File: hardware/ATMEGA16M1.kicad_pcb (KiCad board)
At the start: 2 copper layers, 114.3 x 101.6 mm, 65 parts, among them IC1 ATMEGA16M1-A, IC2 MCP2551-I/SN, J1 PWR, J2 USB, J3 RELAY1, J4 RELAY2, J5 RELAY3, J6 GPIO, J7 AMP/D2A, J8 ADC, J9 CAN, SW1 RESET, U1 NCP1117ST50T3G, U2 FT232RL, U3 RELAY_VO14642AT, U4 RELAY_VO14642AT, U5 RELAY_VO14642AT, X1 16MHz

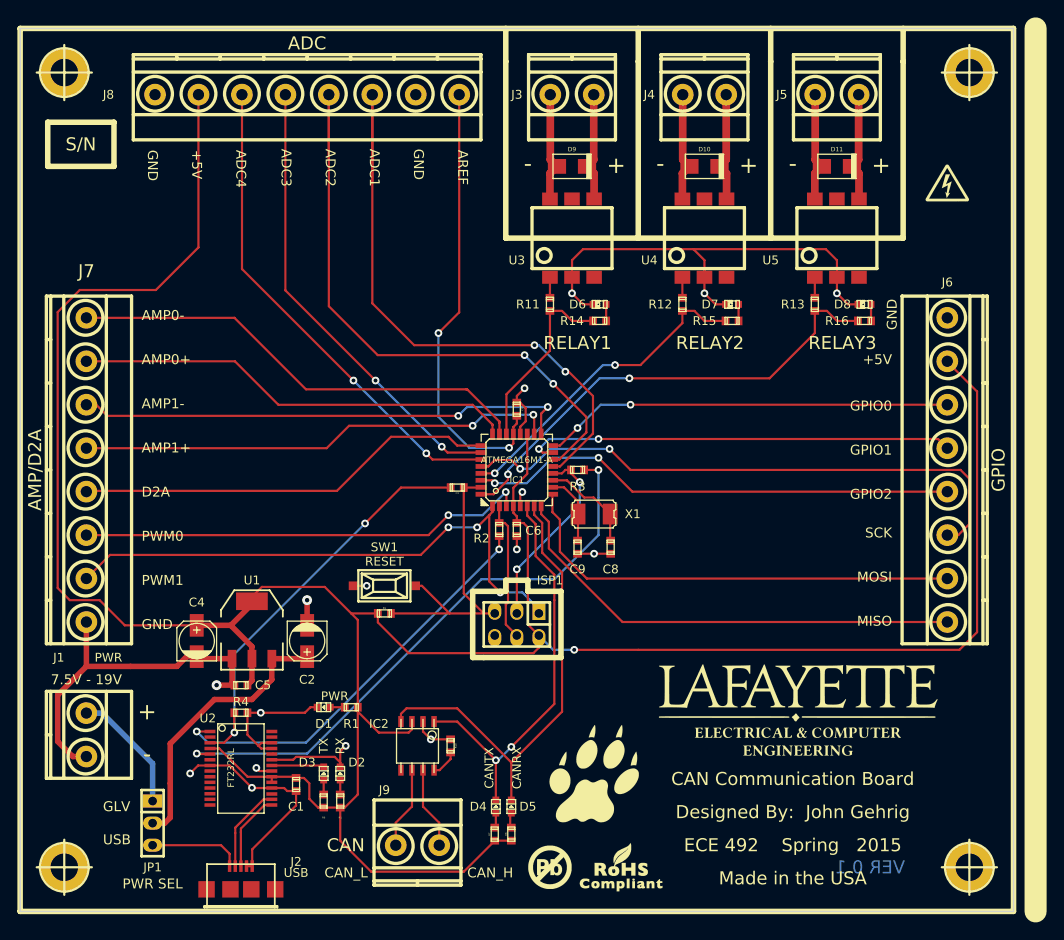
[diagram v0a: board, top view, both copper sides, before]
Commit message: FTDI <-> ISP issue addressed, dip switch added
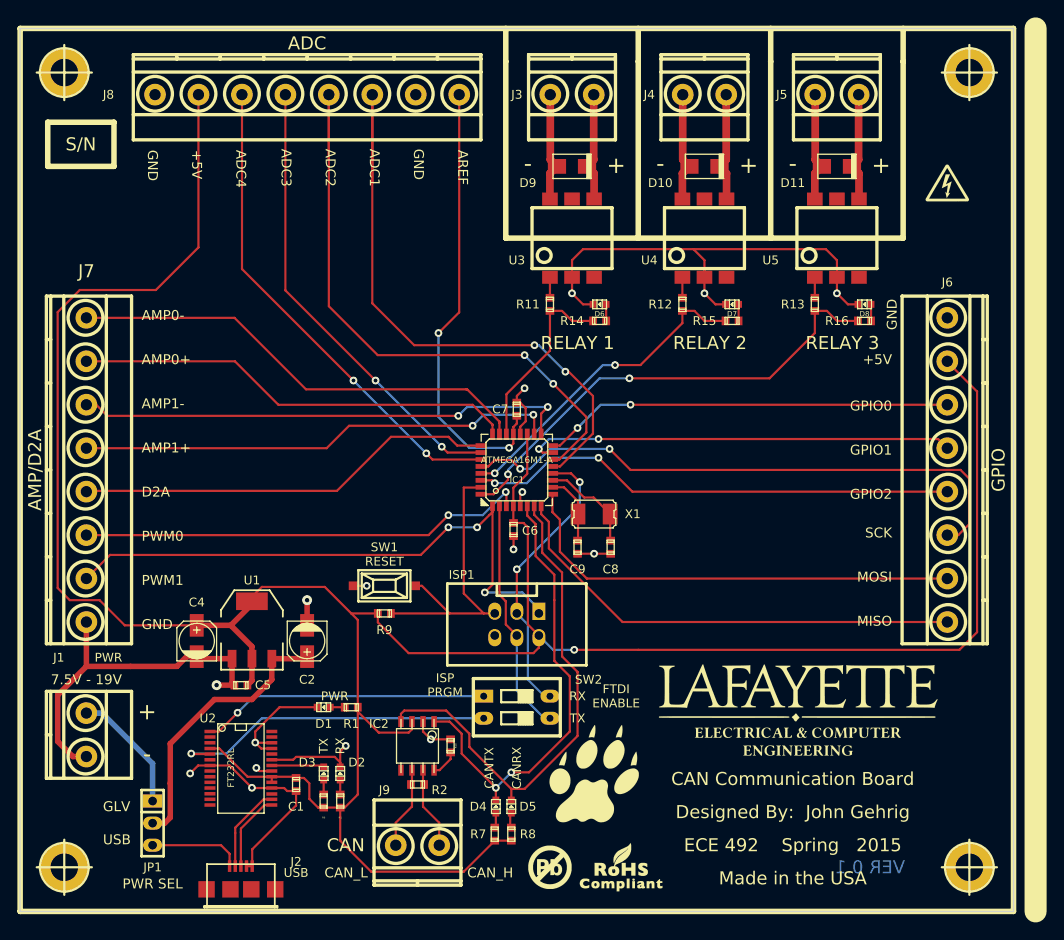
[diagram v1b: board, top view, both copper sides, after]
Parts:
- removed C3: 0.1u, c_0603
- removed R3, R4: 1k, r_0603
- added SW2: FTDI, dip_2-300, F.Cu at (100.3, 123.8)
- C1: value C -> 0.1u
- C5: value 0.1 -> 0.1u
- C8, C9: value 22p -> 10p
- D6, D7, D8: footprint LED-0603 -> Led_0603
- ISP1: footprint pin_strip_3x2 -> vasch_strip_3x2
- J3: value RELAY1 -> RELAY 1
- J4: value RELAY2 -> RELAY 2
- J5: value RELAY3 -> RELAY 3
- R2: value 1k -> 120
- moved R2 30.8 mm to (88.9, 132.7), turned to 0 degrees
- moved C6 0.38 mm to (99.9, 103.4)
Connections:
- R2 pad 1: /FTDI_TX -> /CAN_H
- R2 pad 2: /MOSI_A -> /CAN_L
- U2 pad 3: /RTS -> (no net)
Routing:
- net /RTS: track 47.5 -> 0.00 mm, vias 2 -> 0
- net /FTDI_RX: track 67.3 -> 37.5 mm, vias 2 -> 1
- net /FTDI_TX: track 47.7 -> 33.2 mm, vias 2 -> 1
- net /RXD: track 22.2 -> 33.1 mm
- net /MOSI_A: track 16.4 -> 27.3 mm
- net /CANTX: track 47.1 -> 52.2 mm
- net /CANRX: track 54.1 -> 58.4 mm
- net /MISO_A: track 65.8 -> 68.5 mm
- net GND: track 160.8 -> 158.8 mm
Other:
- board text added: "FTDI ENABLE"
- board text added: "ISP PRGM"
- board text added: "RX"
- board text added: "TX"

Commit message: Reference designations updated, BOM.csv reflects changes & RTS DTR added
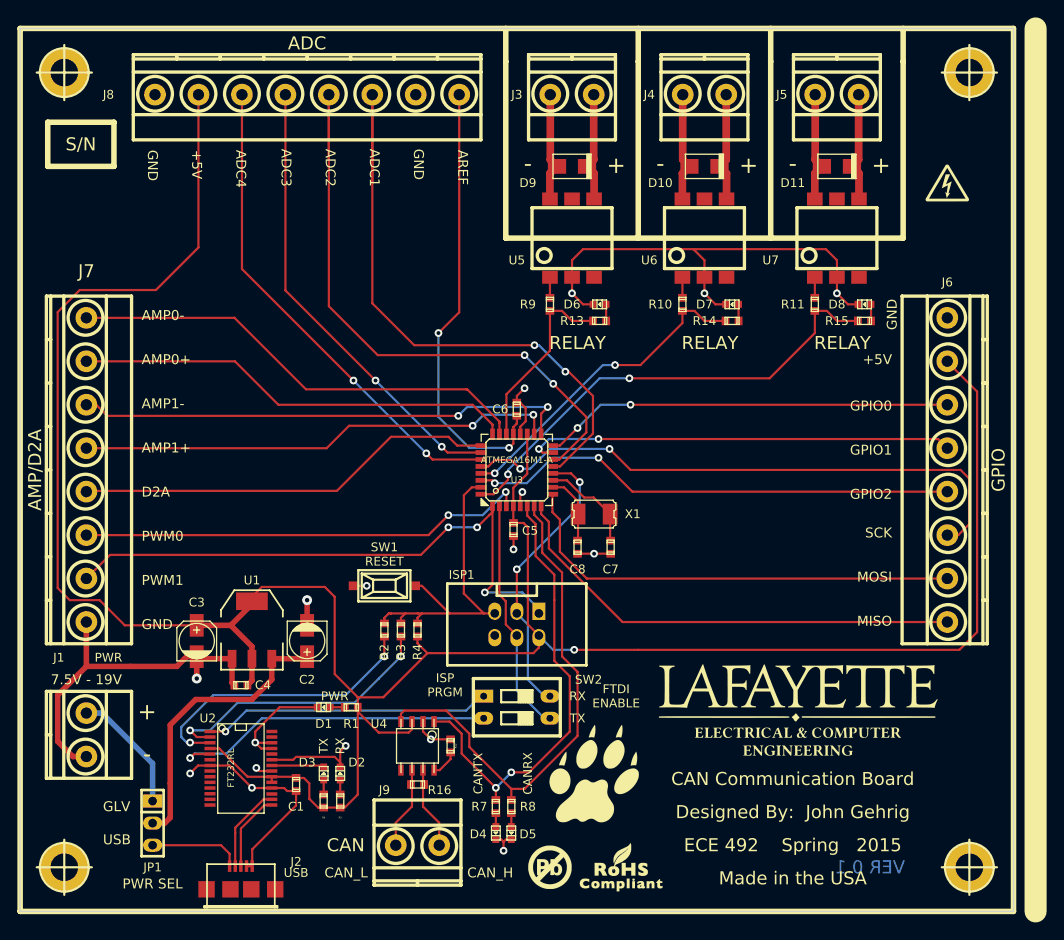
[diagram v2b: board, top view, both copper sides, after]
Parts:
- removed C9: 10p, c_0603
- added C8: 10p, c_0603, F.Cu at (107.3, 105.4)
- added R2: 100, r_0603, F.Cu at (85.1, 114.9)
- added R3: 100, r_0603, F.Cu at (87.0, 114.9)
- J3: value RELAY 1 -> RELAY
- J4: value RELAY 2 -> RELAY
- J5: value RELAY 3 -> RELAY
- moved R4 4.26 mm to (88.9, 114.9), turned to 90 degrees
- moved R7 3.18 mm to (97.9, 135.3)
- moved R8 3.18 mm to (99.7, 135.3)
- moved D4 3.05 mm to (97.9, 138.3), turned to 270 degrees
- moved D5 3.05 mm to (99.7, 138.3), turned to 270 degrees
- renumbered C4 to C3, C5 to C4, C6 to C5, C7 to C6, C8 to C7, R12 to R10, R13 to R11, R10 to R12, R14 to R13, R15 to R14, R16 to R15, R2 to R16, R9 to R4, R11 to R9, IC1 to U3, IC2 to U4, U3 to U5, U4 to U6, U5 to U7
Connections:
- D4 pad 1: N-0000051 -> N-0000052
- D4 pad 2: /CANTX -> GND
- D5 pad 1: N-0000052 -> N-0000053
- D5 pad 2: /CANRX -> GND
- R7 pad 1: N-0000051 -> /CANTX
- R7 pad 2: VCC -> N-0000052
- R8 pad 1: N-0000052 -> /CANRX
- R8 pad 2: VCC -> N-0000053
- U2 pad 2: (no net) -> /DTR
- U2 pad 3: (no net) -> /RTS
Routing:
- net /RTS: track 0.00 -> 33.7 mm, vias 0 -> 2
- net /DTR: track 0.00 -> 32.7 mm, vias 0 -> 2
- net VCC: track 330.2 -> 305.0 mm
- net /~RESET: track 34.6 -> 38.5 mm
- net GND: track 158.8 -> 162.3 mm, vias 15 -> 16
- net N-0000051: track 1.67 -> 0.00 mm
- net N-0000053: track 0.00 -> 1.55 mm
- net /V_USER: track 32.1 -> 33.4 mm
- net /FTDI_RX: track 37.5 -> 38.2 mm

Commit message: gerbers (ver 0.2) sent for fabrication
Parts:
- J3: value RELAY -> RELAY1
- J4: value RELAY -> RELAY2
- J5: value RELAY -> RELAY3
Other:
- board text added: "GPIO3"
- board text added: "MISO/GPIO6"
- board text added: "MOSI/GPIO5"
- board text added: "SCK/GPIO4"
- board text added: "VER 0.2"
- board text removed: "GPIO0"
- board text removed: "MISO"
- board text removed: "MOSI"
- board text removed: "SCK"
- board text removed: "VER 0.1"
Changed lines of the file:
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@@
     (links 136)
     (no_connects 0)
-    (area 43.129999 45.669999 157.530001 147.370001)
+    (area 31.064288 35.250001 161.290001 148.590001)
     (thickness 1.6)
     (drawings 74)
@@
       (drillshape 0)
       (scaleselection 1)
-      (outputdirectory ../../../owncloud/Project/School/vscada/repo/can-embd/hardware/gerber/))
+      (outputdirectory ./gerber/ver-0.2/single/))
   )
   (net 0 "")
@@
       (effects (font (size 1.016 1.016) (thickness 0.2032)))
     )
-    (fp_text value RELAY (at -0.635 -28.575 180) (layer F.SilkS)
+    (fp_text value RELAY1 (at -0.635 -28.575 180) (layer F.SilkS)
       (effects (font (size 1.5 1.5) (thickness 0.3)))
     )
@@
       (effects (font (size 1.016 1.016) (thickness 0.2032)))
     )
-    (fp_text value RELAY (at -0.635 -28.575 180) (layer F.SilkS)
+    (fp_text value RELAY2 (at -0.635 -28.575 180) (layer F.SilkS)
       (effects (font (size 1.5 1.5) (thickness 0.3)))
     )
@@
       (effects (font (size 1.016 1.016) (thickness 0.2032)))
     )
-    (fp_text value RELAY (at -0.635 -28.575 180) (layer F.SilkS)
+    (fp_text value RELAY3 (at -0.635 -28.575 180) (layer F.SilkS)
       (effects (font (size 1.5 1.5) (thickness 0.3)))
     )
@@
     (effects (font (size 1.5 1.5) (thickness 0.3)))
   )
-  (gr_text "VER 0.1" (at 140.97 142.24) (layer B.Cu)
+  (gr_text "VER 0.2" (at 140.97 142.24) (layer B.Cu)
     (effects (font (size 1.5 1.5) (thickness 0.3)) (justify mirror))
   )
@@
   (gr_line (start 129.54 69.85) (end 144.78 69.85) (angle 90) (layer F.SilkS) (width 0.635))
   (gr_line (start 129.54 49.53) (end 129.54 69.85) (angle 90) (layer F.SilkS) (width 0.635))
-  (gr_text MISO (at 143.51 113.919) (layer F.SilkS)
+  (gr_text MISO/GPIO6 (at 143.51 113.919) (layer F.SilkS)
     (effects (font (size 1.143 1.143) (thickness 0.1905)) (justify right))
   )
-  (gr_text GPIO2 (at 143.51 99.314) (layer F.SilkS)
+  (gr_text GPIO3 (at 143.51 99.314) (layer F.SilkS)
     (effects (font (size 1.143 1.143) (thickness 0.1905)) (justify right))
   )
-  (gr_text GPIO0 (at 143.51 89.154) (layer F.SilkS)
+  (gr_text GPIO1 (at 143.51 89.154) (layer F.SilkS)
     (effects (font (size 1.143 1.143) (thickness 0.1905)) (justify right))
   )
-  (gr_text GPIO1 (at 143.51 94.234) (layer F.SilkS)
+  (gr_text GPIO2 (at 143.51 94.234) (layer F.SilkS)
     (effects (font (size 1.143 1.143) (thickness 0.1905)) (justify right))
   )
-  (gr_text SCK (at 143.51 103.759) (layer F.SilkS)
+  (gr_text SCK/GPIO4 (at 143.51 103.759) (layer F.SilkS)
     (effects (font (size 1.143 1.143) (thickness 0.1905)) (justify right))
   )
-  (gr_text MOSI (at 143.51 108.839) (layer F.SilkS)
+  (gr_text MOSI/GPIO5 (at 143.51 108.839) (layer F.SilkS)
     (effects (font (size 1.143 1.143) (thickness 0.1905)) (justify right))
   )
@@
   (segment (start 72.136 118.237) (end 75.96886 118.237) (width 0.635) (layer F.Cu) (net 44))
   (segment (start 75.96886 118.237) (end 76.2 118.00586) (width 0.635) (layer F.Cu) (net 44))
-  (segment (start 96.23044 98.51898) (end 95.15602 98.51898) (width 0.254) (layer F.Cu) (net 45) (status 400000))
+  (segment (start 96.23044 98.51898) (end 95.15602 98.51898) (width 0.254) (layer F.Cu) (net 45))
   (segment (start 94.234 99.441) (end 94.234 110.744) (width 0.254) (layer F.Cu) (net 45))
   (segment (start 95.15602 98.51898) (end 94.234 99.441) (width 0.254) (layer F.Cu) (net 45))
